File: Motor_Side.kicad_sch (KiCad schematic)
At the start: 34 parts, among them Q2 IRLML0030, Q3 IRLML0030, U2 TLV9301xDCK, U3 TLV9301xDCK, U4 TCMT1106, U5 TCMT1106

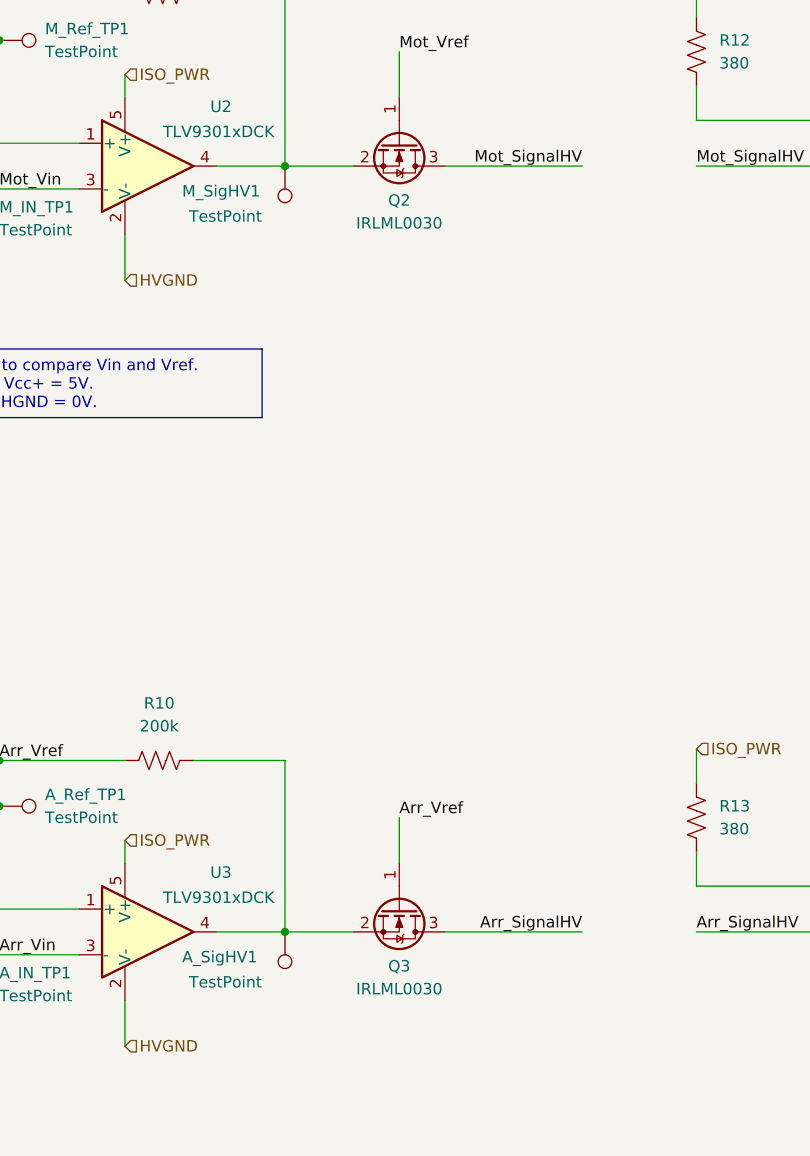
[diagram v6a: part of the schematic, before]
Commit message: fixed HV layout and added the both nmos
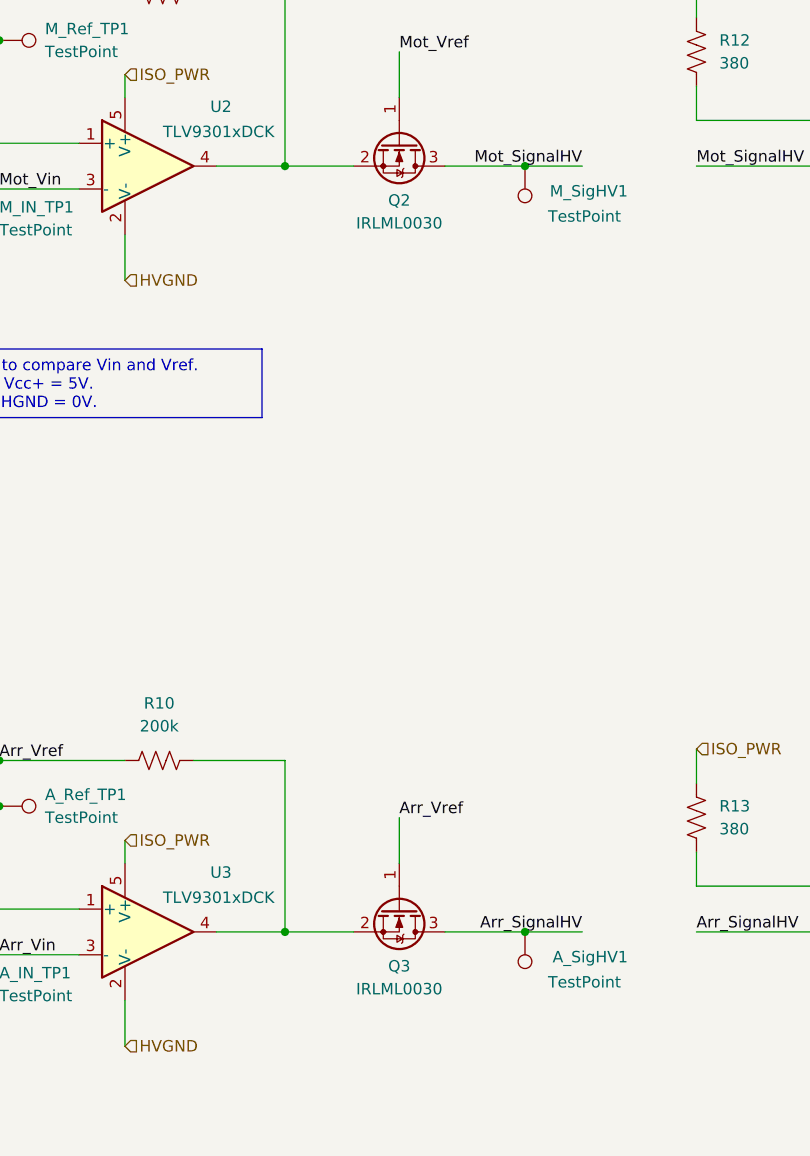
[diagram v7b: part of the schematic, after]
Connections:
- net Arr_SignalHV: now also A_SigHV1.1
- net Mot_SignalHV: now also M_SigHV1.1
- net at Q3.2 (S), R10.1, U3.4: no longer A_SigHV1.1
- net at Q2.2 (S), R5.1, U2.4: no longer M_SigHV1.1
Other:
- moved on the sheet: A_SigHV1, M_SigHV1
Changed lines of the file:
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@@
+	)
+	(junction
+		(at 134.62 57.15)
+		(diameter 0)
+		(color 0 0 0 0)
 	)
 	(junction
@@
 	)
 	(junction
+		(at 134.62 142.24)
+		(diameter 0)
+		(color 0 0 0 0)
+	)
+	(junction
 		(at 66.04 59.69)
 		(diameter 0)
@@
 	(wire
 		(pts
+			(xy 134.62 57.15) (xy 140.97 57.15)
+		)
+		(stroke
+			(width 0)
+			(type default)
+		)
+	)
+	(wire
+		(pts
 			(xy 212.09 142.24) (xy 212.09 144.78)
 		)
@@
 	(wire
 		(pts
+			(xy 134.62 142.24) (xy 140.97 142.24)
+		)
+		(stroke
+			(width 0)
+			(type default)
+		)
+	)
+	(wire
+		(pts
 			(xy 66.04 123.19) (xy 66.04 125.73)
 		)
@@
 	(wire
 		(pts
-			(xy 125.73 142.24) (xy 140.97 142.24)
+			(xy 125.73 142.24) (xy 134.62 142.24)
 		)
 		(stroke
@@
 	(wire
 		(pts
-			(xy 125.73 57.15) (xy 140.97 57.15)
+			(xy 125.73 57.15) (xy 134.62 57.15)
 		)
 		(stroke
@@
 	(symbol
 		(lib_id "Connector:TestPoint")
-		(at 107.95 57.15 180)
+		(at 134.62 57.15 0)
+		(mirror x)
 		(unit 1)
 		(exclude_from_sim no)
@@
 		(dnp no)
 		(property "Reference" "M_SigHV1"
-			(at 96.52 59.944 0)
+			(at 146.05 59.944 0)
 			(effects
 				(font
@@
 		)
 		(property "Value" "TestPoint"
-			(at 97.282 62.738 0)
+			(at 145.288 62.738 0)
 			(effects
 				(font
@@
 		)
 		(property "Footprint" "utsvt-special:TestPoint_HEX_3mmID"
-			(at 102.87 57.15 0)
+			(at 139.7 57.15 0)
 			(effects
 				(font
@@
 		)
 		(property "Datasheet" "~"
-			(at 102.87 57.15 0)
+			(at 139.7 57.15 0)
 			(effects
 				(font
@@
 		)
 		(property "Description" "test point"
-			(at 107.95 57.15 0)
+			(at 134.62 57.15 0)
 			(effects
 				(font
@@
 	(symbol
 		(lib_id "Connector:TestPoint")
-		(at 107.95 142.24 180)
+		(at 134.62 142.24 0)
+		(mirror x)
 		(unit 1)
 		(exclude_from_sim no)
@@
 		(dnp no)
 		(property "Reference" "A_SigHV1"
-			(at 96.52 145.034 0)
+			(at 146.05 145.034 0)
 			(effects
 				(font
@@
 		)
 		(property "Value" "TestPoint"
-			(at 97.282 147.828 0)
+			(at 145.288 147.828 0)
 			(effects
 				(font
@@
 		)
 		(property "Footprint" "utsvt-special:TestPoint_HEX_3mmID"
-			(at 102.87 142.24 0)
+			(at 139.7 142.24 0)
 			(effects
 				(font
@@
 		)
 		(property "Datasheet" "~"
-			(at 102.87 142.24 0)
+			(at 139.7 142.24 0)
 			(effects
 				(font
@@
 		)
 		(property "Description" "test point"
-			(at 107.95 142.24 0)
-			(effects
-				(font
+			(at 134.62 142.24 0)
+			(effects
+				(font

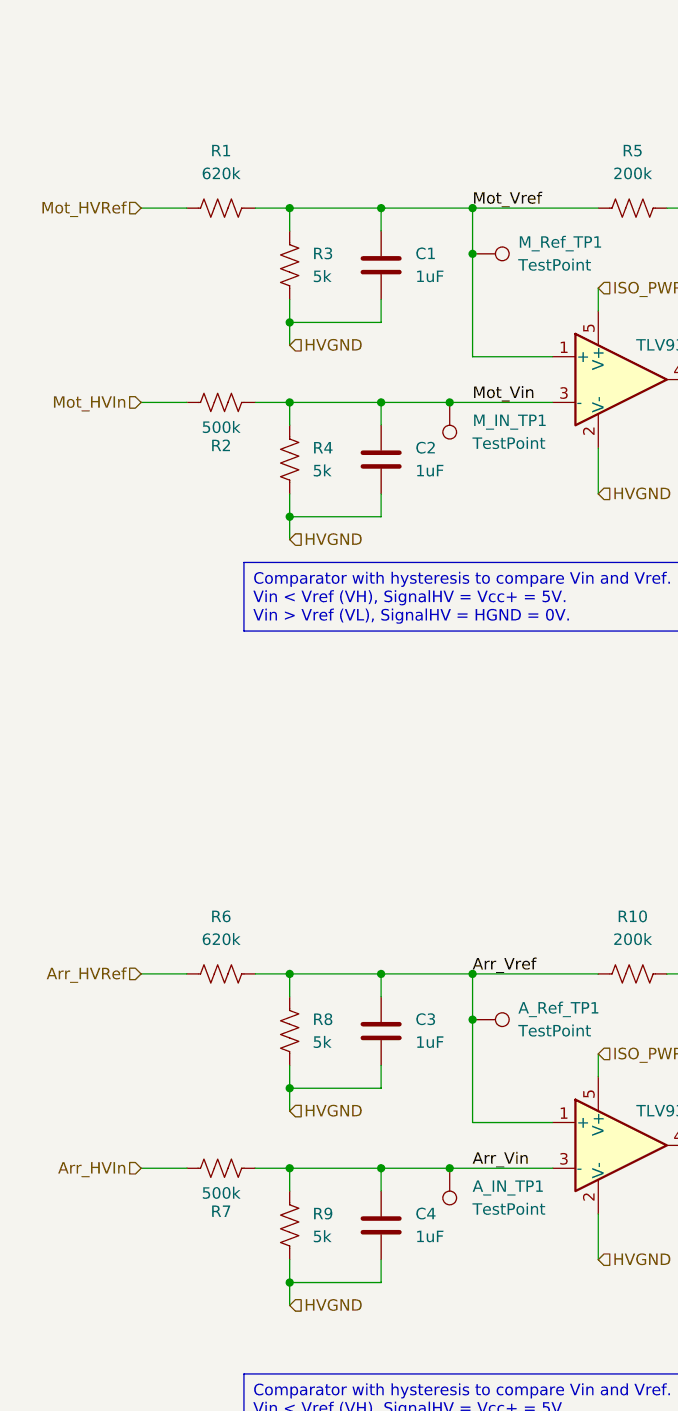
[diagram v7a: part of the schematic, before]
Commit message: changed more resistor values on SCH
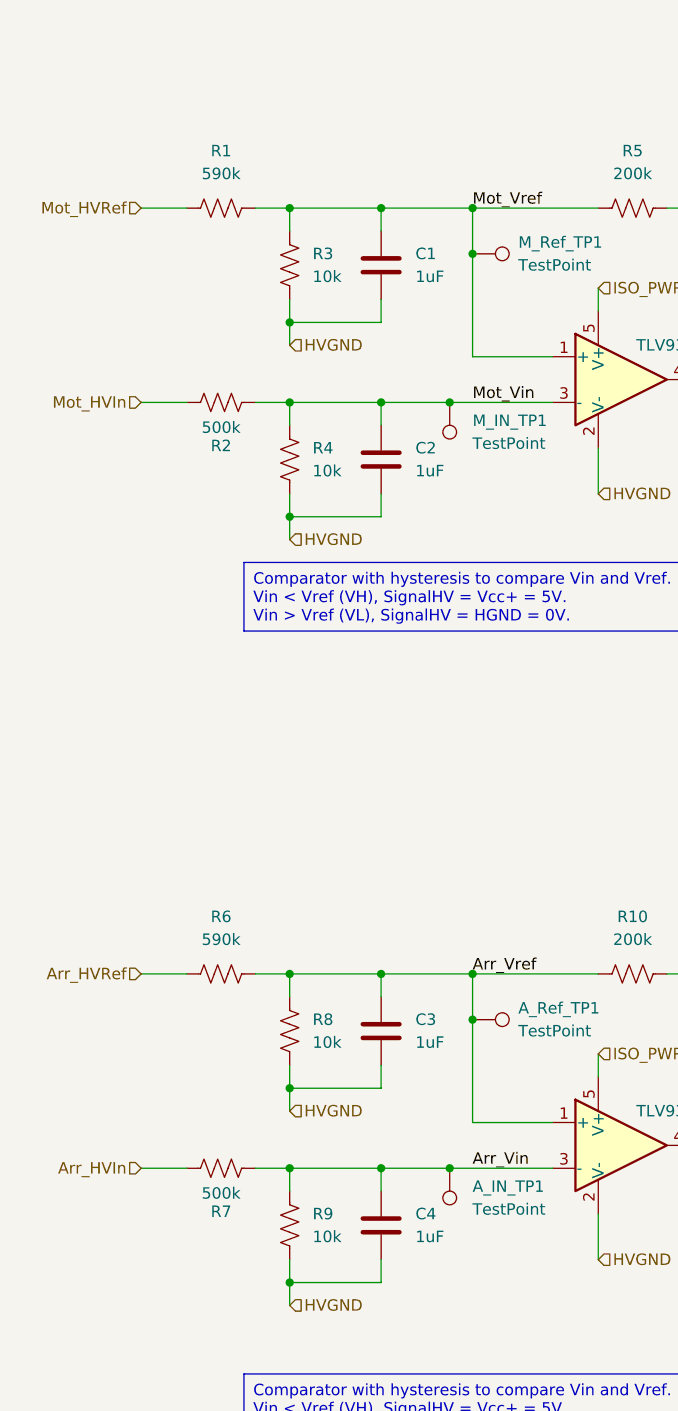
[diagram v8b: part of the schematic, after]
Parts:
- R1, R6: value 620k -> 590k
- R3, R4, R8, R9: value 5k -> 10k
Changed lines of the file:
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@@
 			)
 		)
-		(property "Value" "5k"
+		(property "Value" "10k"
 			(at 58.42 130.8099 0)
 			(effects
@@
 			)
 		)
-		(property "Value" "620k"
+		(property "Value" "590k"
 			(at 48.26 119.38 90)
 			(effects
@@
 			)
 		)
-		(property "Value" "5k"
+		(property "Value" "10k"
 			(at 58.42 67.3099 0)
 			(effects
@@
 			)
 		)
-		(property "Value" "620k"
+		(property "Value" "590k"
 			(at 48.26 34.29 90)
 			(effects
@@
 			)
 		)
-		(property "Value" "5k"
+		(property "Value" "10k"
 			(at 58.42 45.7199 0)
 			(effects
@@
 			)
 		)
-		(property "Value" "5k"
+		(property "Value" "10k"
 			(at 58.42 152.3999 0)
 			(effects
